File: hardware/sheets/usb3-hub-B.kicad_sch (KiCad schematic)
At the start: 28 parts, among them U2 USB5744/2G, Y2 25MHz CL=20pF

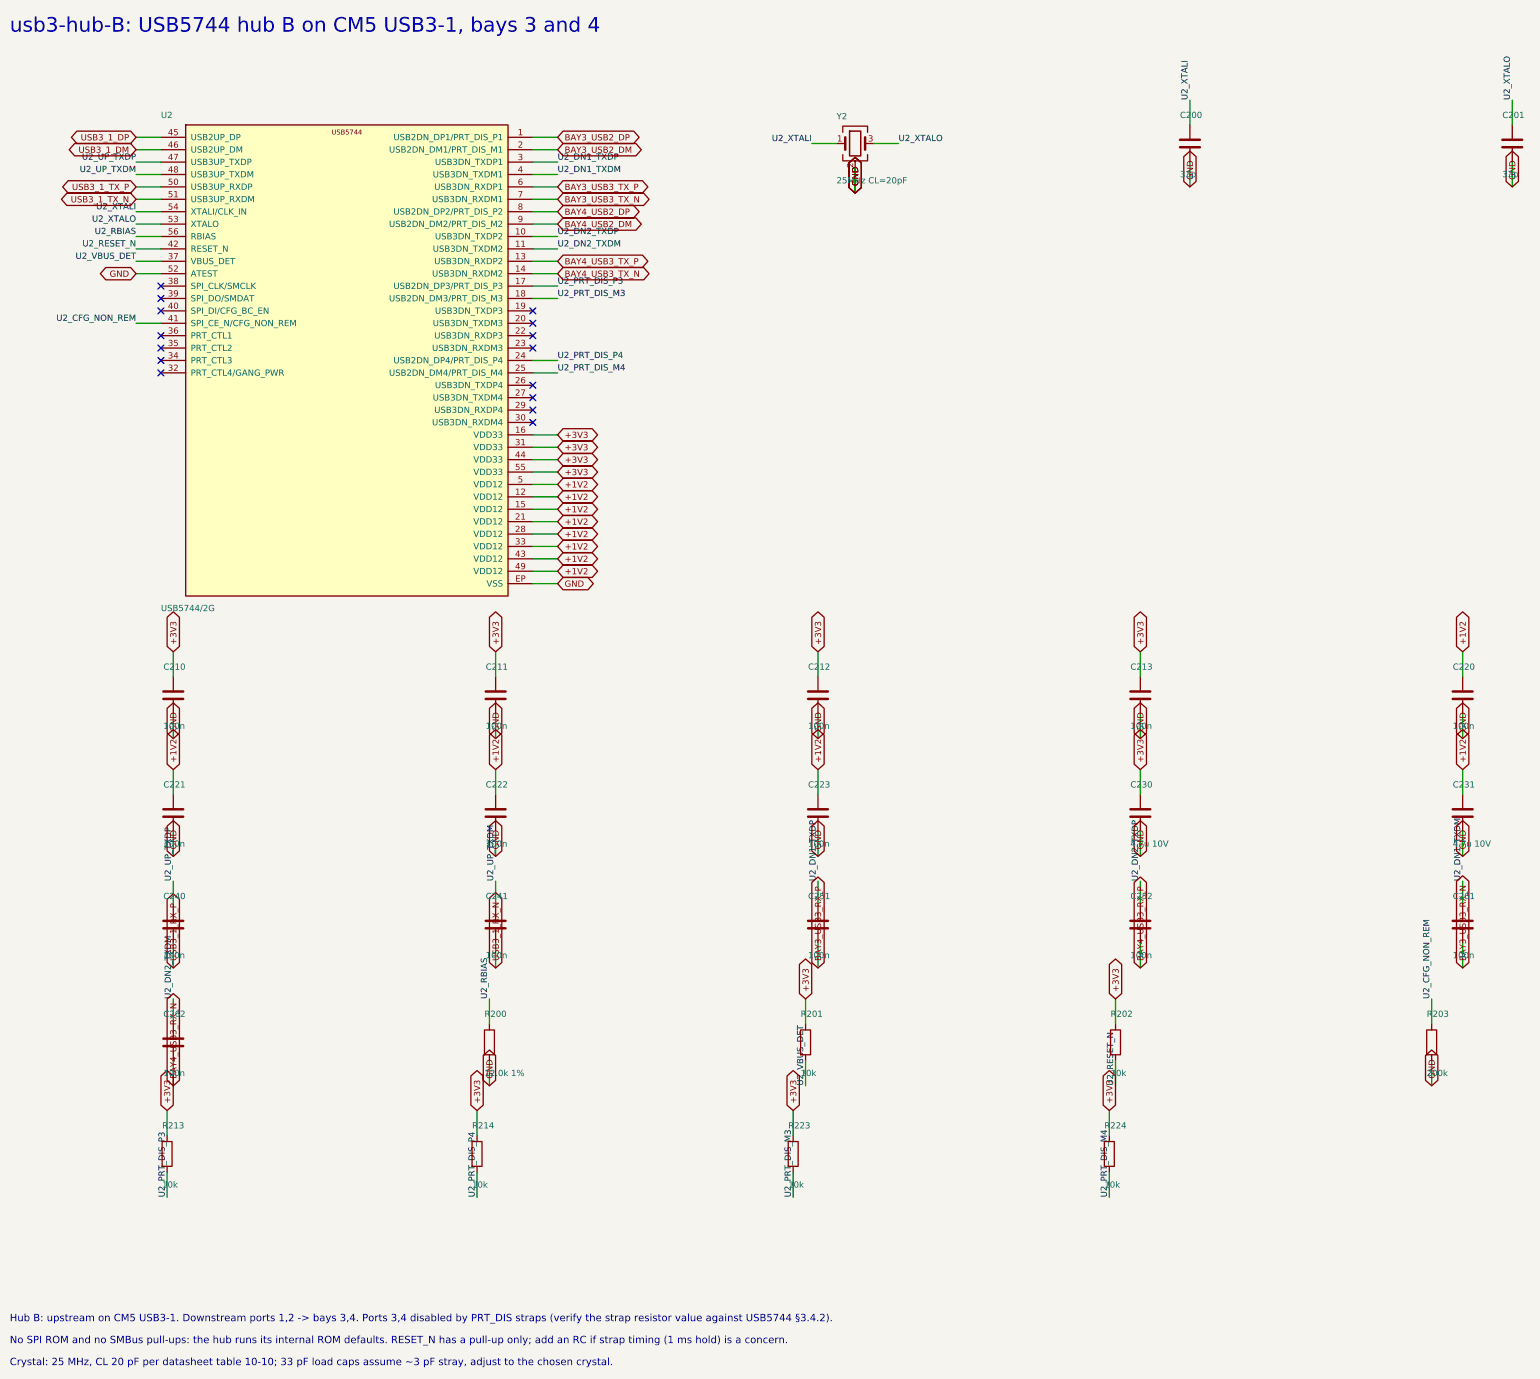
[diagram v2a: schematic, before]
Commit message: docs: C24 brain + bay cards — decisions, architecture, BOM card table, fabrication, README, USAGE, STATUS, changelog, history; diagrams: 8 slots, lid plan, left wall
Co-Authored-By: Claude Fable 5.1 <noreply@anthropic.com>
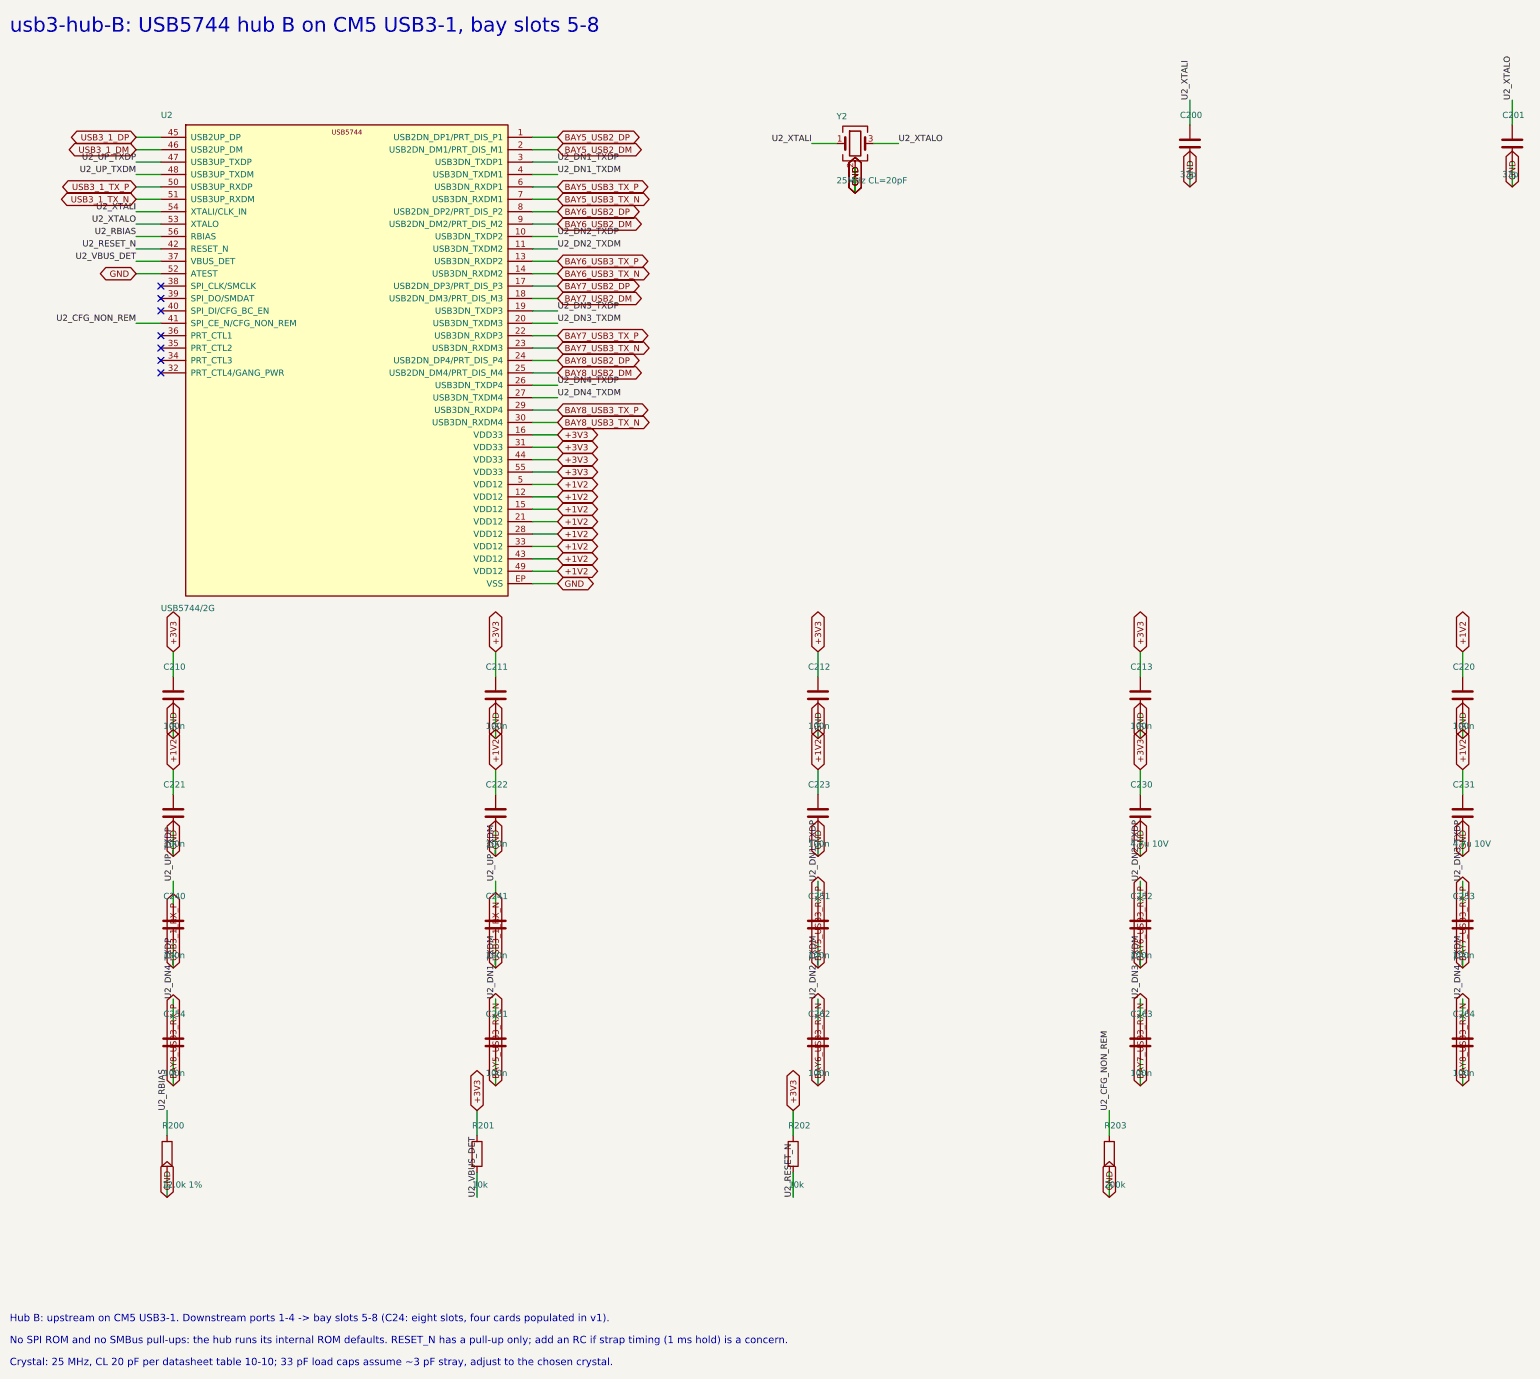
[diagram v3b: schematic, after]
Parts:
- C261: renamed from R200; value 12.0k 1% -> 100n; footprint Resistor_SMD:R_0402_1005Metric -> Capacitor_SMD:C_0402_1005Metric; symbol Device:R -> Device:C
- C262: renamed from R201; value 10k -> 100n; footprint Resistor_SMD:R_0402_1005Metric -> Capacitor_SMD:C_0402_1005Metric; symbol Device:R -> Device:C
- C263: renamed from R202; value 10k -> 100n; footprint Resistor_SMD:R_0402_1005Metric -> Capacitor_SMD:C_0402_1005Metric; symbol Device:R -> Device:C
- C264: renamed from R203; value 200k -> 100n; footprint Resistor_SMD:R_0402_1005Metric -> Capacitor_SMD:C_0402_1005Metric; symbol Device:R -> Device:C
- R200: renamed from R213; value 10k -> 12.0k 1%
- R203: renamed from R224; value 10k -> 200k
- renumbered C261 to C253, C262 to C254, R214 to R201, R223 to R202
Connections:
- net +3V3: no longer C262.1, C263.1, R200.1, R203.1
- net GND: now also R200.2, R203.2; no longer C261.2, C264.2
- net U2_CFG_NON_REM: now also R203.1; no longer C264.1
- net U2_DN1_TXDM: now also C261.1; no longer C253.1
- net U2_DN2_TXDM: now also C262.1; no longer C254.1
- net U2_RBIAS: now also R200.1; no longer C261.1
- net U2_RESET_N: now also R202.2; no longer C263.2
- net U2_VBUS_DET: now also R201.2; no longer C262.2
- net U2_DN3_TXDP: now reaches U2.19 (USB3DN_TXDP3)
- net U2_DN3_TXDP: now also C253.1
- net U2_DN3_TXDM: now reaches U2.20 (USB3DN_TXDM3)
- net U2_DN3_TXDM: now also C263.1
- net BAY7_USB3_TX_P: now reaches U2.22 (USB3DN_RXDP3)
- net BAY7_USB3_TX_N: now reaches U2.23 (USB3DN_RXDM3)
- net U2_DN4_TXDP: now reaches U2.26 (USB3DN_TXDP4)
- net U2_DN4_TXDP: now also C254.1
- net U2_DN4_TXDM: now reaches U2.27 (USB3DN_TXDM4)
- net U2_DN4_TXDM: now also C264.1
- net BAY8_USB3_TX_P: now reaches U2.29 (USB3DN_RXDP4)
- net BAY8_USB3_TX_N: now reaches U2.30 (USB3DN_RXDM4)
- net BAY3_USB2_DM renamed BAY5_USB2_DM
- net BAY3_USB2_DP renamed BAY5_USB2_DP
- net BAY3_USB3_RX_N renamed BAY7_USB3_RX_P
- net BAY3_USB3_RX_P renamed BAY5_USB3_RX_P
- net BAY3_USB3_TX_N renamed BAY5_USB3_TX_N
- net BAY3_USB3_TX_P renamed BAY5_USB3_TX_P
- net BAY4_USB2_DM renamed BAY6_USB2_DM
- net BAY4_USB2_DP renamed BAY6_USB2_DP
- net BAY4_USB3_RX_N renamed BAY8_USB3_RX_P
- net BAY4_USB3_RX_P renamed BAY6_USB3_RX_P
- net BAY4_USB3_TX_N renamed BAY6_USB3_TX_N
- net BAY4_USB3_TX_P renamed BAY6_USB3_TX_P
- net U2_PRT_DIS_M3 renamed BAY7_USB2_DM
- net BAY7_USB2_DM: no longer R202.2
- net U2_PRT_DIS_M4 renamed BAY8_USB2_DM
- net BAY8_USB2_DM: no longer R203.2
- net U2_PRT_DIS_P3 renamed BAY7_USB2_DP
- net BAY7_USB2_DP: no longer R200.2
- net U2_PRT_DIS_P4 renamed BAY8_USB2_DP
- net BAY8_USB2_DP: no longer R201.2
- new net BAY5_USB3_RX_N: C261.2
- new net BAY6_USB3_RX_N: C262.2
- new net BAY7_USB3_RX_N: C263.2
- new net BAY8_USB3_RX_N: C264.2
- no-connect marks 15 -> 7
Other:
- note added: "Hub B: upstream on CM5 USB3-1. Downstream ports 1-4 -> bay slots 5-8 (C24: eight slots, four cards populated in v1)."
- note added: "usb3-hub-B: USB5744 hub B on CM5 USB3-1, bay slots 5-8"
- note removed: "Hub B: upstream on CM5 USB3-1. Downstream ports 1,2 -> bays 3,4. Ports 3,4 disabled by PRT_DIS straps (verify the strap resistor value against USB5744 §3.4.2)."
- note removed: "usb3-hub-B: USB5744 hub B on CM5 USB3-1, bays 3 and 4"
